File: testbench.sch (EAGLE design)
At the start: 47 parts, among them T1 C8492, T2 C8492, T3 C8545, T4 C8545, X1 MKDSN1,5/2-5,08

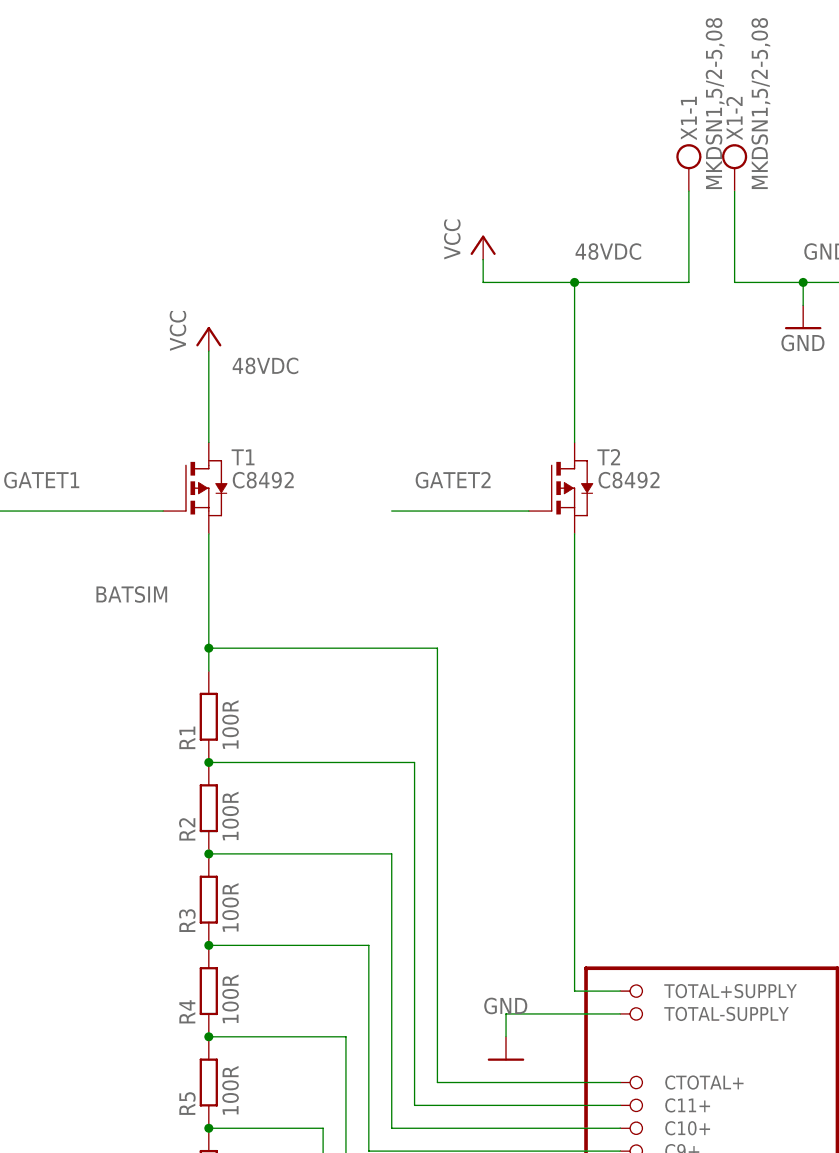
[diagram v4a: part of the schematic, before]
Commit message: fixed PFETs reverse orientation, v1.2
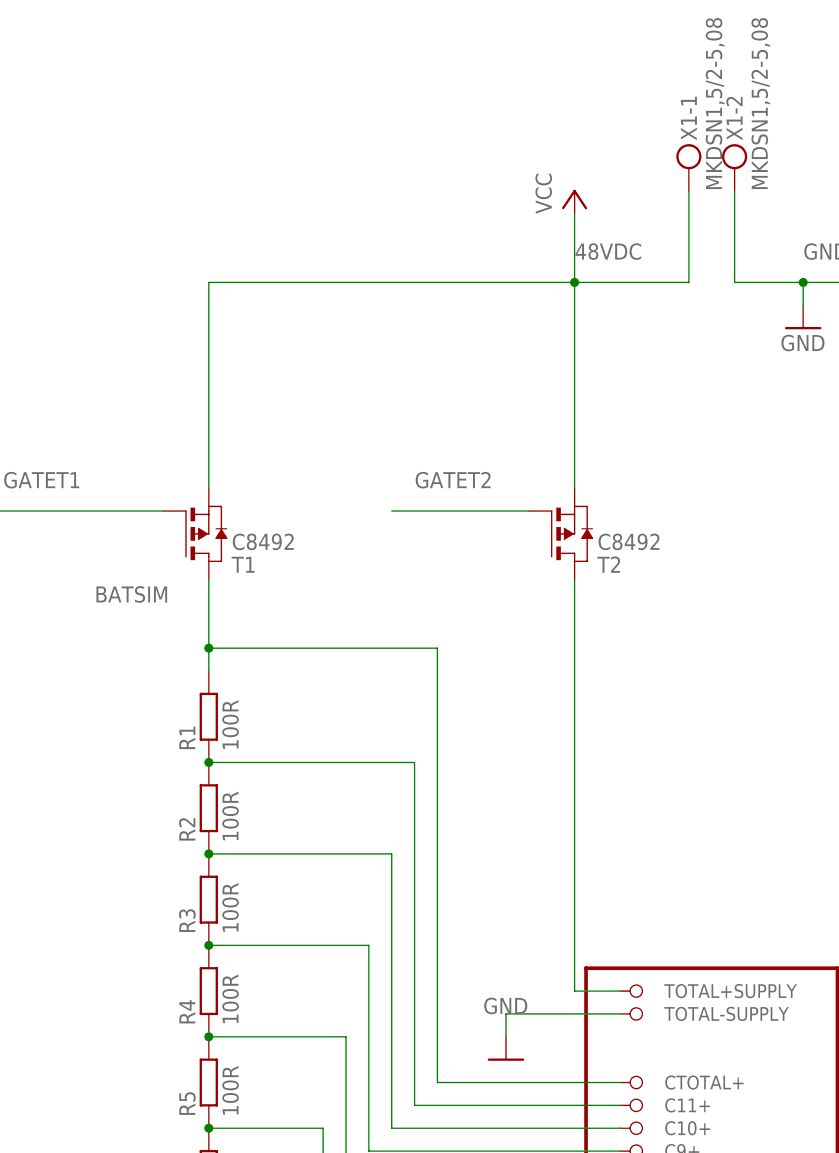
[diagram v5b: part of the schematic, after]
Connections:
- net 48VDC: now also T1.S, T2.S; no longer T1.D, T2.D
- net BATSIM: now also T1.D; no longer T1.S
- net N$19: now also T2.D; no longer T2.S
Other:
- moved on the sheet: T1, T2
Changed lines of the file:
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@@
 <part name="GND1" library="supply1" library_urn="urn:adsk.eagle:library:371" deviceset="GND" device=""/>
 <part name="P+1" library="supply1" library_urn="urn:adsk.eagle:library:371" deviceset="VCC" device=""/>
-<part name="P+2" library="supply1" library_urn="urn:adsk.eagle:library:371" deviceset="VCC" device=""/>
 <part name="U$1" library="diy-modules" deviceset="DC-DC-STEP-DOWN-LM2596HVS" device=""/>
 <part name="P+3" library="supply1" library_urn="urn:adsk.eagle:library:371" deviceset="+5V" device=""/>
@@
 <attribute name="VALUE" x="114.3" y="182.88" size="1.778" layer="96"/>
 </instance>
-<instance part="P+1" gate="VCC" x="81.28" y="195.58" smashed="yes">
-<attribute name="VALUE" x="78.74" y="193.04" size="1.778" layer="96" rot="R90"/>
-</instance>
-<instance part="P+2" gate="VCC" x="50.8" y="185.42" smashed="yes">
-<attribute name="VALUE" x="48.26" y="182.88" size="1.778" layer="96" rot="R90"/>
+<instance part="P+1" gate="VCC" x="91.44" y="200.66" smashed="yes">
+<attribute name="VALUE" x="88.9" y="198.12" size="1.778" layer="96" rot="R90"/>
 </instance>
 <instance part="U$1" gate="G$1" x="190.5" y="195.58" smashed="yes">
@@
 <attribute name="VALUE" x="87.63" y="61.722" size="1.778" layer="96" rot="R180"/>
 </instance>
-<instance part="T1" gate="A" x="50.8" y="167.64" smashed="yes">
-<attribute name="VALUE" x="53.34" y="167.64" size="1.778" layer="96"/>
-<attribute name="NAME" x="53.34" y="170.18" size="1.778" layer="95"/>
-</instance>
-<instance part="T2" gate="A" x="91.44" y="167.64" smashed="yes">
-<attribute name="VALUE" x="93.98" y="167.64" size="1.778" layer="96"/>
-<attribute name="NAME" x="93.98" y="170.18" size="1.778" layer="95"/>
+<instance part="T1" gate="A" x="50.8" y="162.56" smashed="yes" rot="MR180">
+<attribute name="VALUE" x="53.34" y="162.56" size="1.778" layer="96" rot="MR180"/>
+<attribute name="NAME" x="53.34" y="160.02" size="1.778" layer="95" rot="MR180"/>
+</instance>
+<instance part="T2" gate="A" x="91.44" y="162.56" smashed="yes" rot="MR180">
+<attribute name="VALUE" x="93.98" y="162.56" size="1.778" layer="96" rot="MR180"/>
+<attribute name="NAME" x="93.98" y="160.02" size="1.778" layer="95" rot="MR180"/>
 </instance>
 <instance part="T3" gate="A" x="-43.18" y="93.98" smashed="yes">
@@
 <label x="91.44" y="193.04" size="1.778" layer="95"/>
 <pinref part="P+1" gate="VCC" pin="VCC"/>
-<wire x1="91.44" y1="190.5" x2="81.28" y2="190.5" width="0.1524" layer="91"/>
-<wire x1="81.28" y1="190.5" x2="81.28" y2="193.04" width="0.1524" layer="91"/>
-<pinref part="T2" gate="A" pin="D"/>
-<wire x1="91.44" y1="172.72" x2="91.44" y2="190.5" width="0.1524" layer="91"/>
+<wire x1="91.44" y1="190.5" x2="91.44" y2="198.12" width="0.1524" layer="91"/>
+<pinref part="T2" gate="A" pin="S"/>
+<wire x1="91.44" y1="167.64" x2="91.44" y2="190.5" width="0.1524" layer="91"/>
 <junction x="91.44" y="190.5"/>
+<pinref part="T1" gate="A" pin="S"/>
+<wire x1="50.8" y1="167.64" x2="50.8" y2="190.5" width="0.1524" layer="91"/>
+<wire x1="91.44" y1="190.5" x2="50.8" y2="190.5" width="0.1524" layer="91"/>
 </segment>
 <segment>
@@
 <wire x1="172.72" y1="200.66" x2="157.48" y2="200.66" width="0.1524" layer="91"/>
 <label x="157.48" y="200.66" size="1.778" layer="95"/>
-</segment>
-<segment>
-<pinref part="T1" gate="A" pin="D"/>
-<pinref part="P+2" gate="VCC" pin="VCC"/>
-<wire x1="50.8" y1="172.72" x2="50.8" y2="182.88" width="0.1524" layer="91"/>
-<label x="53.34" y="180.34" size="1.778" layer="95"/>
 </segment>
 <segment>
@@
 <pinref part="JP1" gate="G$1" pin="TOTAL+SUPPLY"/>
 <wire x1="96.52" y1="111.76" x2="91.44" y2="111.76" width="0.1524" layer="91"/>
-<pinref part="T2" gate="A" pin="S"/>
-<wire x1="91.44" y1="111.76" x2="91.44" y2="162.56" width="0.1524" layer="91"/>
+<pinref part="T2" gate="A" pin="D"/>
+<wire x1="91.44" y1="111.76" x2="91.44" y2="157.48" width="0.1524" layer="91"/>
 </segment>
 </net>
@@
 <wire x1="76.2" y1="101.6" x2="76.2" y2="149.86" width="0.1524" layer="91"/>
 <wire x1="76.2" y1="149.86" x2="50.8" y2="149.86" width="0.1524" layer="91"/>
-<pinref part="T1" gate="A" pin="S"/>
-<wire x1="50.8" y1="162.56" x2="50.8" y2="149.86" width="0.1524" layer="91"/>
+<label x="38.1" y="154.94" size="1.778" layer="95"/>
+<pinref part="T1" gate="A" pin="D"/>
+<wire x1="50.8" y1="149.86" x2="50.8" y2="157.48" width="0.1524" layer="91"/>
 <junction x="50.8" y="149.86"/>
-<label x="38.1" y="154.94" size="1.778" layer="95"/>
-</segment>
-</net>
+</segment>
+</net>

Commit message: new smd footprint of BMS connector integrated
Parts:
- JP1: device pinhead_own:PINHD-2X11_MEB12S_MODULSEITE -> pinhead_own:PINHD-2X11_MEB12S_MODULSEITE_SMD
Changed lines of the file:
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@@
 <part name="R17" library="rcl" library_urn="urn:adsk.eagle:library:334" deviceset="R-EU_" device="R0805" package3d_urn="urn:adsk.eagle:package:23553/2" value="680R"/>
 <part name="R18" library="rcl" library_urn="urn:adsk.eagle:library:334" deviceset="R-EU_" device="R0805" package3d_urn="urn:adsk.eagle:package:23553/2" value="680R"/>
-<part name="JP1" library="pinhead_own" deviceset="PINHD-2X11_MEB12S_MODULSEITE" device=""/>
+<part name="JP1" library="pinhead_own" deviceset="PINHD-2X11_MEB12S_MODULSEITE" device="_SMD"/>
 <part name="GND5" library="supply1" library_urn="urn:adsk.eagle:library:371" deviceset="GND" device=""/>
 <part name="GND6" library="supply1" library_urn="urn:adsk.eagle:library:371" deviceset="GND" device=""/>
